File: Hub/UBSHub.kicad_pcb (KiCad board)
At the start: 2 copper layers, 106.9 x 68.6 mm, 102 parts, among them J1 Conn_02x03_Odd_Even, J10 2Port_USB2_0, J11 2Port_USB2_0, J12 2Port_USB2_0, J13 Barrel_Jack, J14 ESP32_PRG, J2 Conn_01x02, J3 DB9_Male, J4 DB9_Male, J5 Conn_02x03_Odd_Even, J6 Joy1, J7 Conn_01x02, J8 Joy2, J9 USB_B_Micro, SW1 328RST, SW2 RST_FE2.1, U1 ATmega328P-AU, U2 ATmega328P-AU, U3 Terminus_Technology_FE2.1, U4 MCP1703A-3302_SOT23, U5 ESP32-WROOM, X1 12MHz, X2 12MHz, X3 12MHz

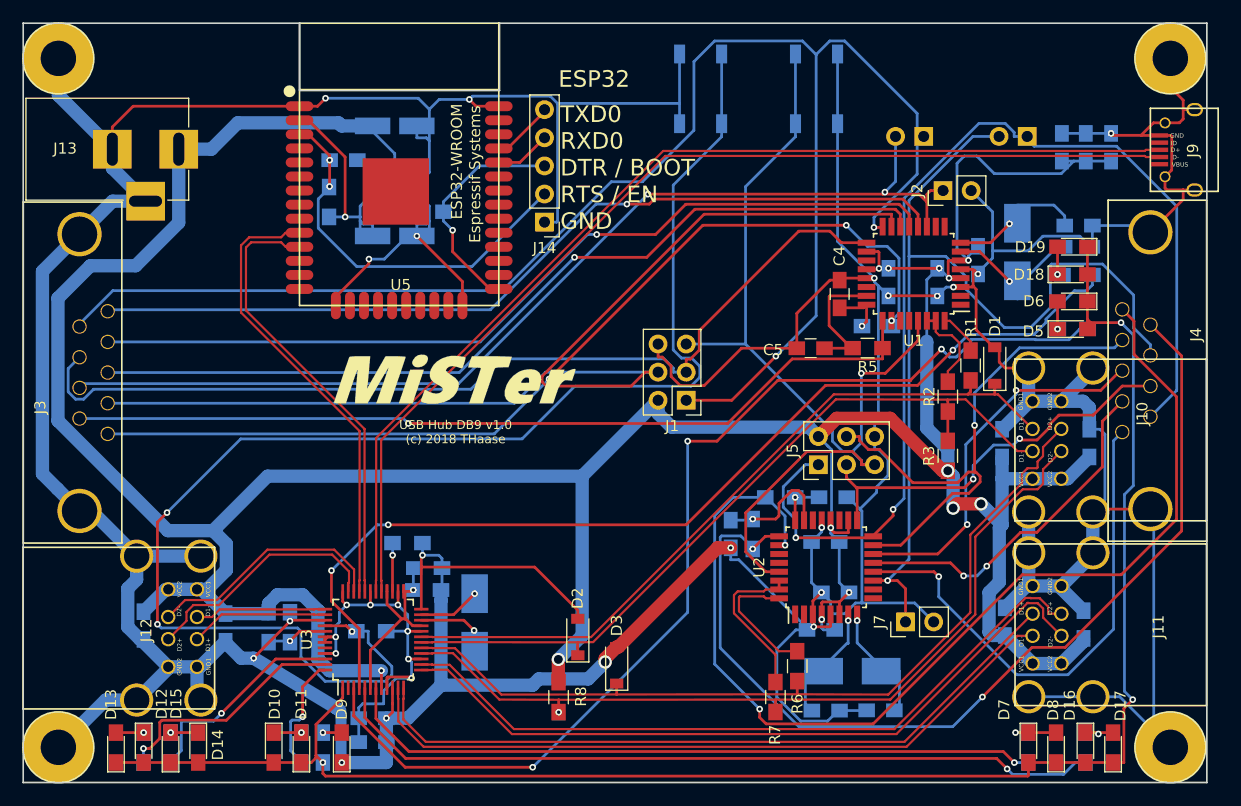
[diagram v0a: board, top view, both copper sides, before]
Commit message: add some missing data / add forgotten pullup for ESP32
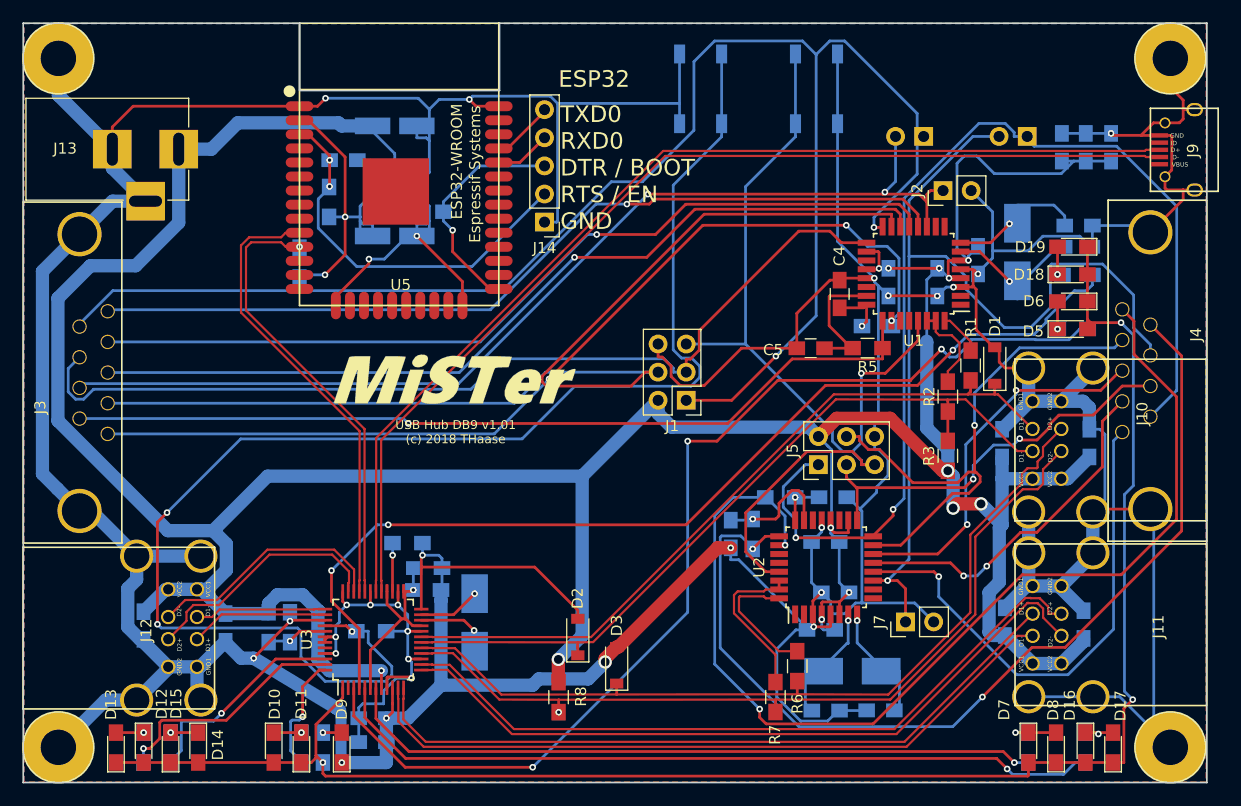
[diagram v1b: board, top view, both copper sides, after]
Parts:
- added R25: 1k8, Resistors_SMD:R_0805_HandSoldering, B.Cu at (116.9, 82.7)
- J2: value Conn_01x02 -> Joy1
- J3: value DB9_Male -> Joy1
- J4: value DB9_Male -> Joy2
- J7: value Conn_01x02 -> Joy2
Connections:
- net /USBHubOSC/XTAL3_1 renamed /USBHubPower/XTAL3_1
- net /USBHubOSC/XTAL3_2 renamed /USBHubPower/XTAL3_2
- net Net-(R22-Pad2) renamed /USBHubPower/FE_2_1_RST
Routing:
- net /ESP32/ESP32_V3_3: track 25.4 -> 33.8 mm, vias 1 -> 2
- net D5-: vias 0 -> 1
- added copper zone on B.Cu, net GND
- added copper zone on F.Cu, net GND
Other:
- board text added: "USB Hub DB9 v1.01 (c) 2018 THaase"
- board text removed: "USB Hub DB9 v1.0 (c) 2018 THaase"
